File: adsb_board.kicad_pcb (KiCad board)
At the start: 2 copper layers, 50 x 25 mm, 14 parts, among them J1 Conn_Coaxial, J2 Conn_Coaxial, J3 USB_B_Micro, U1 TA1090EC, U2 TA1090EC, U3 PSA4-5043+

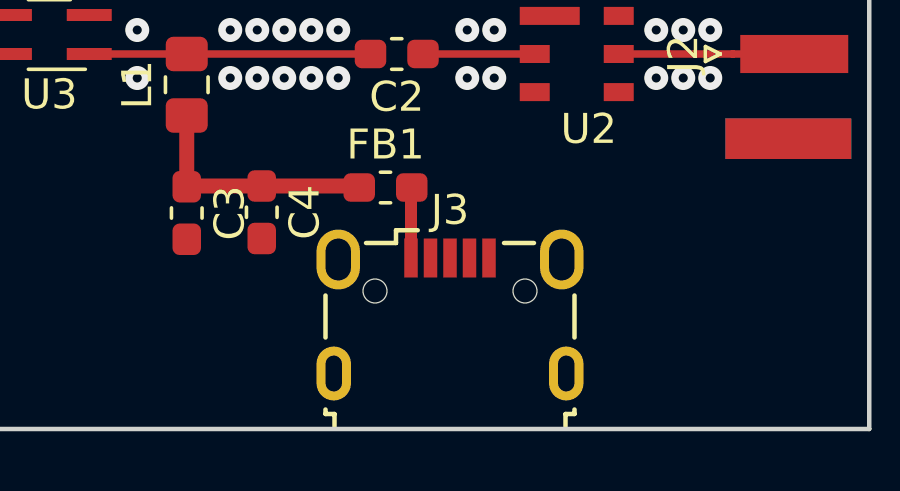
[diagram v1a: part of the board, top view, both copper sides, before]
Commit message: change usb connector to type with circular holes
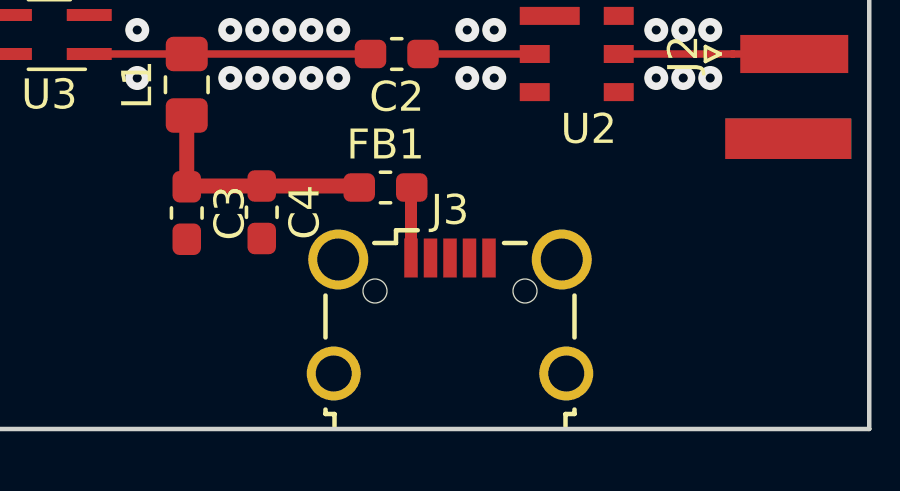
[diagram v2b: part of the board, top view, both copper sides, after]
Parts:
- J3: footprint Connector_USB:USB_Micro-B_Wuerth_629105150521 -> Connector_USB:USB_Micro-B_Wuerth_629105150521_CircularHoles
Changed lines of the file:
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@@
     (35 F.Paste user hide)
     (36 B.SilkS user hide)
-    (37 F.SilkS user)
+    (37 F.SilkS user hide)
     (38 B.Mask user hide)
     (39 F.Mask user hide)
@@
   )
   (setup
-    (last_trace_width 0.5)
+    (last_trace_width 0.25)
     (user_trace_width 0.3)
     (user_trace_width 0.4)
@@
       (psnegative false)
       (psa4output false)
-      (plotreference true)
-      (plotvalue true)
+      (plotreference false)
+      (plotvalue false)
       (plotinvisibletext false)
-      (padsonsilk false)
+      (padsonsilk true)
       (subtractmaskfromsilk false)
       (outputformat 1)
@@
       (drillshape 0)
       (scaleselection 1)
-      (outputdirectory "../../dump/adsb_test_gerber/"))
+      (outputdirectory "gerber/"))
   )
   (net 0 "")
@@
     (add_net "Net-(U3-Pad4)")
   )
+  (module Connector_USB:USB_Micro-B_Wuerth_629105150521_CircularHoles (layer F.Cu)
+    (at 136.025 96.2)
+    (descr "USB Micro-B receptacle, http://www.mouser.com/ds/2/445/629105150521-469306.pdf")
+    (tags "usb micro receptacle")
+    (attr smd)
+    (fp_text reference J3 (at 0 -3.5) (layer F.SilkS)
+      (effects (font (size 1 1) (thickness 0.15)))
+    )
+    (fp_text value USB_B_Micro (at 0 5.6) (layer F.Fab)
+      (effects (font (size 1 1) (thickness 0.15)))
+    )
+    (fp_line (start -4 -2.25) (end -4 3.15) (layer F.Fab) (width 0.15))
+    (fp_line (start -4 3.15) (end -3.7 3.15) (layer F.Fab) (width 0.15))
+    (fp_line (start -3.7 3.15) (end -3.7 4.35) (layer F.Fab) (width 0.15))
+    (fp_line (start -3.7 4.35) (end 3.7 4.35) (layer F.Fab) (width 0.15))
+    (fp_line (start 3.7 4.35) (end 3.7 3.15) (layer F.Fab) (width 0.15))
+    (fp_line (start 3.7 3.15) (end 4 3.15) (layer F.Fab) (width 0.15))
+    (fp_line (start 4 3.15) (end 4 -2.25) (layer F.Fab) (width 0.15))
+    (fp_line (start 4 -2.25) (end -4 -2.25) (layer F.Fab) (width 0.15))
+    (fp_line (start -2.7 3.75) (end 2.7 3.75) (layer F.Fab) (width 0.15))
+    (fp_line (start -1.075 -2.725) (end -1.3 -2.55) (layer F.Fab) (width 0.15))
+    (fp_line (start -1.3 -2.55) (end -1.525 -2.725) (layer F.Fab) (width 0.15))
+    (fp_line (start -1.525 -2.725) (end -1.525 -2.95) (layer F.Fab) (width 0.15))
+    (fp_line (start -1.525 -2.95) (end -1.075 -2.95) (layer F.Fab) (width 0.15))
+    (fp_line (start -1.075 -2.95) (end -1.075 -2.725) (layer F.Fab) (width 0.15))
+    (fp_line (start -4.15 -0.65) (end -4.15 0.75) (layer F.SilkS) (width 0.15))
+    (fp_line (start -4.15 3.15) (end -4.15 3.3) (layer F.SilkS) (width 0.15))
+    (fp_line (start -4.15 3.3) (end -3.85 3.3) (layer F.SilkS) (width 0.15))
+    (fp_line (start -3.85 3.3) (end -3.85 3.75) (layer F.SilkS) (width 0.15))
+    (fp_line (start 3.85 3.75) (end 3.85 3.3) (layer F.SilkS) (width 0.15))
+    (fp_line (start 3.85 3.3) (end 4.15 3.3) (layer F.SilkS) (width 0.15))
+    (fp_line (start 4.15 3.3) (end 4.15 3.15) (layer F.SilkS) (width 0.15))
+    (fp_line (start 4.15 0.75) (end 4.15 -0.65) (layer F.SilkS) (width 0.15))
+    (fp_line (start -1.075 -2.825) (end -1.8 -2.825) (layer F.SilkS) (width 0.15))
+    (fp_line (start -1.8 -2.825) (end -1.8 -2.4) (layer F.SilkS) (width 0.15))
+    (fp_line (start -1.8 -2.4) (end -2.525 -2.4) (layer F.SilkS) (width 0.15))
+    (fp_line (start 1.8 -2.4) (end 2.525 -2.4) (layer F.SilkS) (width 0.15))
+    (fp_line (start -5.27 -3.34) (end -5.27 4.85) (layer F.CrtYd) (width 0.05))
+    (fp_line (start -5.27 4.85) (end 5.28 4.85) (layer F.CrtYd) (width 0.05))
+    (fp_line (start 5.28 4.85) (end 5.28 -3.34) (layer F.CrtYd) (width 0.05))
+    (fp_line (start 5.28 -3.34) (end -5.27 -3.34) (layer F.CrtYd) (width 0.05))
+    (fp_text user %R (at 0 1.05) (layer F.Fab)
+      (effects (font (size 1 1) (thickness 0.15)))
+    )
+    (fp_text user "PCB Edge" (at 0 3.75) (layer Dwgs.User)
+      (effects (font (size 0.5 0.5) (thickness 0.08)))
+    )
+    (pad 1 smd rect (at -1.3 -1.9) (size 0.45 1.3) (layers F.Cu F.Paste F.Mask)
+      (net 13 "Net-(FB1-Pad2)"))
+    (pad 2 smd rect (at -0.65 -1.9) (size 0.45 1.3) (layers F.Cu F.Paste F.Mask)
+      (net 10 "Net-(J3-Pad2)"))
+    (pad 3 smd rect (at 0 -1.9) (size 0.45 1.3) (layers F.Cu F.Paste F.Mask)
+      (net 11 "Net-(J3-Pad3)"))
+    (pad 4 smd rect (at 0.65 -1.9) (size 0.45 1.3) (layers F.Cu F.Paste F.Mask)
+      (net 12 "Net-(J3-Pad4)"))
+    (pad 5 smd rect (at 1.3 -1.9) (size 0.45 1.3) (layers F.Cu F.Paste F.Mask)
+      (net 1 /GND))
+    (pad 6 thru_hole circle (at -3.725 -1.85) (size 2 2) (drill 1.4) (layers *.Cu *.Mask)
+      (net 1 /GND))
+    (pad 6 thru_hole circle (at 3.725 -1.85) (size 2 2) (drill 1.4) (layers *.Cu *.Mask)
+      (net 1 /GND))
+    (pad 6 thru_hole circle (at -3.875 1.95) (size 1.8 1.8) (drill 1.2) (layers *.Cu *.Mask)
+      (net 1 /GND))
+    (pad 6 thru_hole circle (at 3.875 1.95) (size 1.8 1.8) (drill 1.2) (layers *.Cu *.Mask)
+      (net 1 /GND))
+    (pad "" np_thru_hole circle (at -2.5 -0.8) (size 0.8 0.8) (drill 0.8) (layers *.Cu *.Mask))
+    (pad "" np_thru_hole circle (at 2.5 -0.8) (size 0.8 0.8) (drill 0.8) (layers *.Cu *.Mask))
+    (model ${KISYS3DMOD}/Connector_USB.3dshapes/USB_Micro-B_Wuerth_629105150521_CircularHoles.wrl
+      (at (xyz 0 0 0))
+      (scale (xyz 1 1 1))
+      (rotate (xyz 0 0 0))
+    )
+  )
   (module Resistor_SMD:R_0603_1608Metric_Pad1.05x0.95mm_HandSolder (layer F.Cu)
     (at 133.875 91.95)
@@
       (at (xyz 0 0 0))
       (scale (xyz 1 1 1))
-      (rotate (xyz 0 0 0))
-    )
-  )
-  (module Connector_USB:USB_Micro-B_Wuerth_629105150521 (layer F.Cu)
-    (at 136.025 96.2)
-    (descr "USB Micro-B receptacle, http://www.mouser.com/ds/2/445/629105150521-469306.pdf")
-    (tags "usb micro receptacle")
-    (attr smd)
-    (fp_text reference J3 (at 0 -3.5) (layer F.SilkS)
-      (effects (font (size 1 1) (thickness 0.15)))
-    )
-    (fp_text value USB_B_Micro (at 0 5.6) (layer F.Fab)
-      (effects (font (size 1 1) (thickness 0.15)))
-    )
-    (fp_text user "PCB Edge" (at 0 3.75) (layer Dwgs.User)
-      (effects (font (size 0.5 0.5) (thickness 0.08)))
-    )
-    (fp_text user %R (at 0 1.05) (layer F.Fab)
-      (effects (font (size 1 1) (thickness 0.15)))
-    )
-    (fp_line (start 4.95 -3.34) (end -4.94 -3.34) (layer F.CrtYd) (width 0.05))
-    (fp_line (start 4.95 4.85) (end 4.95 -3.34) (layer F.CrtYd) (width 0.05))
-    (fp_line (start -4.94 4.85) (end 4.95 4.85) (layer F.CrtYd) (width 0.05))
-    (fp_line (start -4.94 -3.34) (end -4.94 4.85) (layer F.CrtYd) (width 0.05))
-    (fp_line (start 1.8 -2.4) (end 2.8 -2.4) (layer F.SilkS) (width 0.15))
-    (fp_line (start -1.8 -2.4) (end -2.8 -2.4) (layer F.SilkS) (width 0.15))
-    (fp_line (start -1.8 -2.825) (end -1.8 -2.4) (layer F.SilkS) (width 0.15))
-    (fp_line (start -1.075 -2.825) (end -1.8 -2.825) (layer F.SilkS) (width 0.15))
-    (fp_line (start 4.15 0.75) (end 4.15 -0.65) (layer F.SilkS) (width 0.15))
-    (fp_line (start 4.15 3.3) (end 4.15 3.15) (layer F.SilkS) (width 0.15))
-    (fp_line (start 3.85 3.3) (end 4.15 3.3) (layer F.SilkS) (width 0.15))
-    (fp_line (start 3.85 3.75) (end 3.85 3.3) (layer F.SilkS) (width 0.15))
-    (fp_line (start -3.85 3.3) (end -3.85 3.75) (layer F.SilkS) (width 0.15))
-    (fp_line (start -4.15 3.3) (end -3.85 3.3) (layer F.SilkS) (width 0.15))
-    (fp_line (start -4.15 3.15) (end -4.15 3.3) (layer F.SilkS) (width 0.15))
-    (fp_line (start -4.15 -0.65) (end -4.15 0.75) (layer F.SilkS) (width 0.15))
-    (fp_line (start -1.075 -2.95) (end -1.075 -2.725) (layer F.Fab) (width 0.15))
-    (fp_line (start -1.525 -2.95) (end -1.075 -2.95) (layer F.Fab) (width 0.15))
-    (fp_line (start -1.525 -2.725) (end -1.525 -2.95) (layer F.Fab) (width 0.15))
-    (fp_line (start -1.3 -2.55) (end -1.525 -2.725) (layer F.Fab) (width 0.15))
-    (fp_line (start -1.075 -2.725) (end -1.3 -2.55) (layer F.Fab) (width 0.15))
-    (fp_line (start -2.7 3.75) (end 2.7 3.75) (layer F.Fab) (width 0.15))
-    (fp_line (start 4 -2.25) (end -4 -2.25) (layer F.Fab) (width 0.15))
-    (fp_line (start 4 3.15) (end 4 -2.25) (layer F.Fab) (width 0.15))
-    (fp_line (start 3.7 3.15) (end 4 3.15) (layer F.Fab) (width 0.15))
-    (fp_line (start 3.7 4.35) (end 3.7 3.15) (layer F.Fab) (width 0.15))
-    (fp_line (start -3.7 4.35) (end 3.7 4.35) (layer F.Fab) (width 0.15))
-    (fp_line (start -3.7 3.15) (end -3.7 4.35) (layer F.Fab) (width 0.15))
-    (fp_line (start -4 3.15) (end -3.7 3.15) (layer F.Fab) (width 0.15))
-    (fp_line (start -4 -2.25) (end -4 3.15) (layer F.Fab) (width 0.15))
-    (pad "" np_thru_hole oval (at 2.5 -0.8) (size 0.8 0.8) (drill 0.8) (layers *.Cu *.Mask))
-    (pad "" np_thru_hole oval (at -2.5 -0.8) (size 0.8 0.8) (drill 0.8) (layers *.Cu *.Mask))
-    (pad 6 thru_hole oval (at 3.875 1.95) (size 1.15 1.8) (drill oval 0.55 1.2) (layers *.Cu *.Mask)
-      (net 1 /GND))
-    (pad 6 thru_hole oval (at -3.875 1.95) (size 1.15 1.8) (drill oval 0.55 1.2) (layers *.Cu *.Mask)
-      (net 1 /GND))
-    (pad 6 thru_hole oval (at 3.725 -1.85) (size 1.45 2) (drill oval 0.85 1.4) (layers *.Cu *.Mask)
-      (net 1 /GND))
-    (pad 6 thru_hole oval (at -3.725 -1.85) (size 1.45 2) (drill oval 0.85 1.4) (layers *.Cu *.Mask)
-      (net 1 /GND))
-    (pad 5 smd rect (at 1.3 -1.9) (size 0.45 1.3) (layers F.Cu F.Paste F.Mask)
-      (net 1 /GND))
-    (pad 4 smd rect (at 0.65 -1.9) (size 0.45 1.3) (layers F.Cu F.Paste F.Mask)
-      (net 12 "Net-(J3-Pad4)"))
-    (pad 3 smd rect (at 0 -1.9) (size 0.45 1.3) (layers F.Cu F.Paste F.Mask)
-      (net 11 "Net-(J3-Pad3)"))
-    (pad 2 smd rect (at -0.65 -1.9) (size 0.45 1.3) (layers F.Cu F.Paste F.Mask)
-      (net 10 "Net-(J3-Pad2)"))
-    (pad 1 smd rect (at -1.3 -1.9) (size 0.45 1.3) (layers F.Cu F.Paste F.Mask)
-      (net 13 "Net-(FB1-Pad2)"))
-    (model ${KISYS3DMOD}/Connector_USB.3dshapes/USB_Micro-B_Wuerth_629105150521.wrl
-      (at (xyz 0 0 0))
-      (scale (xyz 1 1 1))

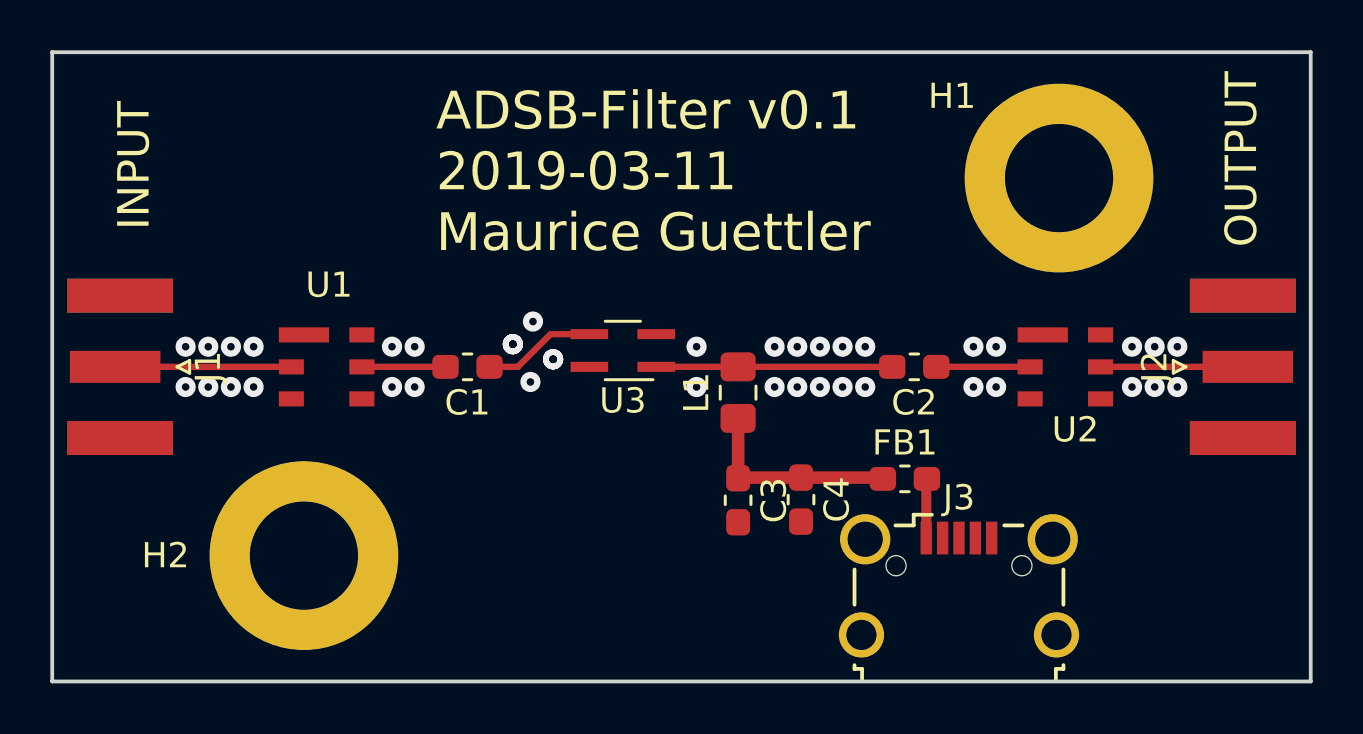
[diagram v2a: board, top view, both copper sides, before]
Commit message: improve silkscreen
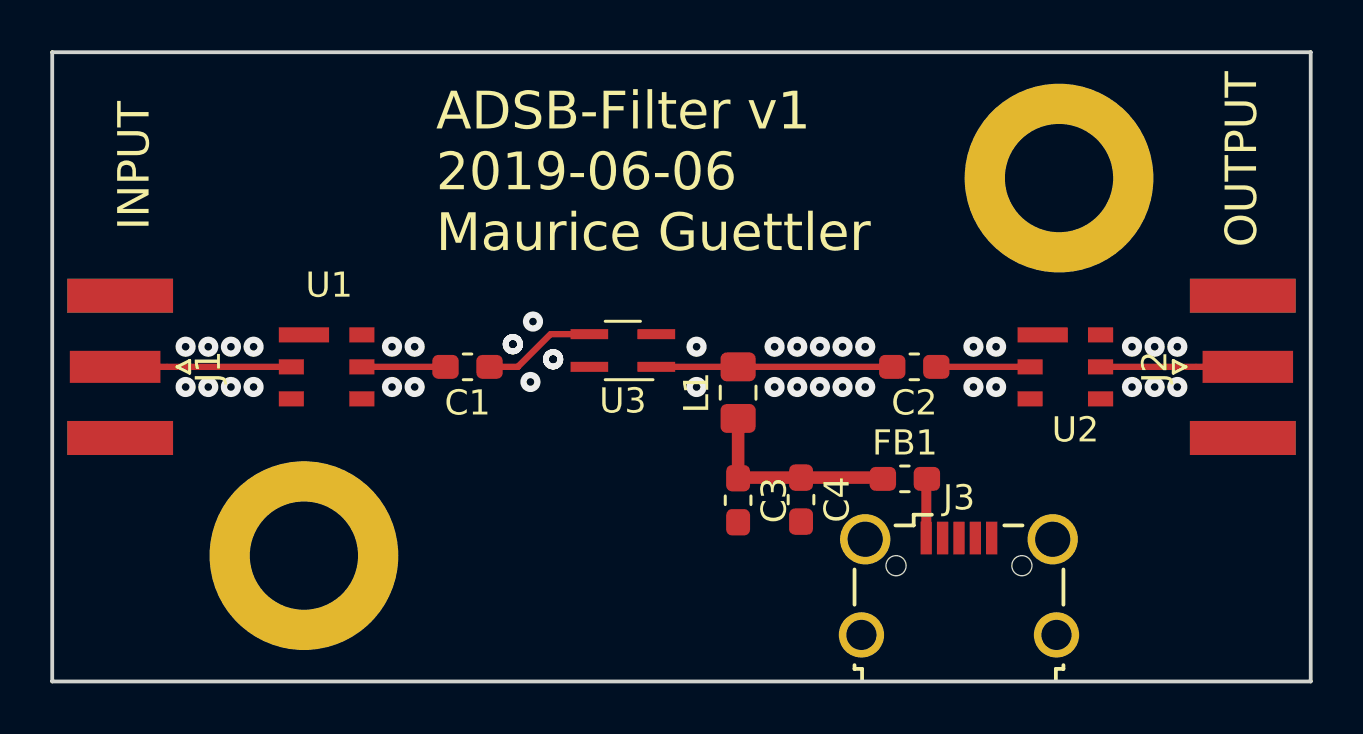
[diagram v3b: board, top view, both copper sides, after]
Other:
- board text added: "ADSB-Filter v1 2019-06-06 Maurice Guettler"
- board text removed: "ADSB-Filter v0.1 2019-03-11 Maurice Guettler"
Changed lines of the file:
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@@
     (35 F.Paste user hide)
     (36 B.SilkS user hide)
-    (37 F.SilkS user hide)
+    (37 F.SilkS user)
     (38 B.Mask user hide)
     (39 F.Mask user hide)
     (40 Dwgs.User user hide)
-    (41 Cmts.User user)
+    (41 Cmts.User user hide)
     (42 Eco1.User user hide)
-    (43 Eco2.User user)
-    (44 Edge.Cuts user)
-    (45 Margin user)
-    (46 B.CrtYd user)
+    (43 Eco2.User user hide)
+    (44 Edge.Cuts user hide)
+    (45 Margin user hide)
+    (46 B.CrtYd user hide)
     (47 F.CrtYd user hide)
-    (48 B.Fab user)
+    (48 B.Fab user hide)
     (49 F.Fab user hide)
   )
@@
       (psnegative false)
       (psa4output false)
-      (plotreference false)
+      (plotreference true)
       (plotvalue false)
       (plotinvisibletext false)
@@
     (tags "mounting hole 4.3mm m4 din965")
     (attr virtual)
-    (fp_text reference H2 (at -5.5 0) (layer F.SilkS)
+    (fp_text reference H2 (at -5.5 0) (layer F.SilkS) hide
       (effects (font (size 1 1) (thickness 0.15)))
     )
@@
     (tags "mounting hole 4.3mm m4 din965")
     (attr virtual)
-    (fp_text reference H1 (at -4.25 -3.25) (layer F.SilkS)
+    (fp_text reference H1 (at -4.25 -3.25) (layer F.SilkS) hide
       (effects (font (size 1 1) (thickness 0.15)))
     )
@@
     (effects (font (size 1.25 1.25) (thickness 0.3)))
   )
-  (gr_text "ADSB-Filter v0.1\n2019-03-11\nMaurice Guettler" (at 115.25 79.75) (layer F.SilkS)
+  (gr_text "ADSB-Filter v1\n2019-06-06\nMaurice Guettler" (at 115.25 79.75) (layer F.SilkS)
     (effects (font (size 1.5 1.5) (thickness 0.3)) (justify left))
   )

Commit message: final changes - move sma connectors to board edge
- changes properties of bottom gnd shape

- move refdes of sma connectors
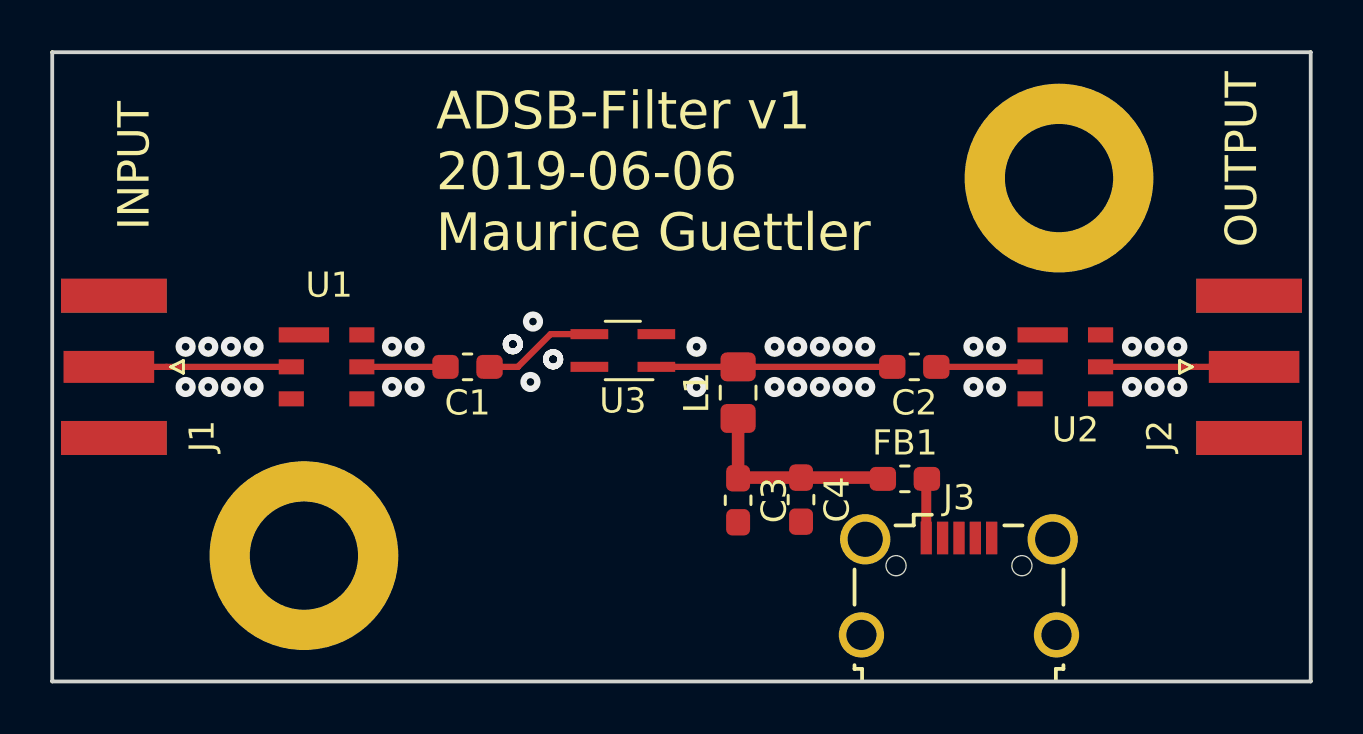
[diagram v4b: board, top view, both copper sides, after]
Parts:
- moved J1 0.25 mm to (102.5, 87.5)
- moved J2 0.25 mm to (147.6, 87.5)
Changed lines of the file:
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@@
     (45 Margin user hide)
     (46 B.CrtYd user hide)
-    (47 F.CrtYd user hide)
+    (47 F.CrtYd user)
     (48 B.Fab user hide)
-    (49 F.Fab user hide)
+    (49 F.Fab user)
   )
   (setup
@@
   )
   (module Connector_Coaxial:SMA_Samtec_SMA-J-P-H-ST-EM1_EdgeMount (layer F.Cu)
-    (at 147.3 87.5)
+    (at 147.55 87.5)
     (descr http://suddendocs.samtec.com/prints/sma-j-p-x-st-em1-mkt.pdf)
     (tags SMA)
     (attr smd)
-    (fp_text reference J2 (at -3.5 0 90) (layer F.SilkS)
+    (fp_text reference J2 (at -3.55 2.75 90) (layer F.SilkS)
       (effects (font (size 1 1) (thickness 0.15)))
     )
@@
   )
   (module Connector_Coaxial:SMA_Samtec_SMA-J-P-H-ST-EM1_EdgeMount (layer F.Cu)
-    (at 102.7 87.5 180)
+    (at 102.45 87.5 180)
     (descr http://suddendocs.samtec.com/prints/sma-j-p-x-st-em1-mkt.pdf)
     (tags SMA)
     (attr smd)
-    (fp_text reference J1 (at -3.5 0 270) (layer F.SilkS)
+    (fp_text reference J1 (at -3.5 -2.75 270) (layer F.SilkS)
       (effects (font (size 1 1) (thickness 0.15)))
     )
@@
   (segment (start 104.55 87.5) (end 109.5 87.5) (width 0.25) (layer F.Cu) (net 2))
   (segment (start 102.5 87.5) (end 104.55 87.5) (width 0.25) (layer F.Cu) (net 2))
+  (segment (start 147.5 87.5) (end 145.45 87.5) (width 0.25) (layer F.Cu) (net 3))
   (segment (start 145.45 87.5) (end 141.65 87.5) (width 0.25) (layer F.Cu) (net 3))
-  (segment (start 147.5 87.5) (end 145.45 87.5) (width 0.25) (layer F.Cu) (net 3))
   (segment (start 132.95 91.9) (end 133 91.95) (width 0.5) (layer F.Cu) (net 4))
   (segment (start 129.75 91.9) (end 132.95 91.9) (width 0.5) (layer F.Cu) (net 4))
@@
   (segment (start 134.725 94.3) (end 134.725 91.975) (width 0.4) (layer F.Cu) (net 13))
   (zone (net 1) (net_name /GND) (layer B.Cu) (hatch edge 0.508)
-    (connect_pads (clearance 0.508))
-    (min_thickness 0.254)
-    (fill yes (arc_segments 16) (thermal_gap 0.508) (thermal_bridge_width 0.508))
+    (connect_pads (clearance 0.2))
+    (min_thickness 0.2)
+    (fill yes (arc_segments 16) (thermal_gap 0.2) (thermal_bridge_width 0.508))
     (polygon
       (pts
